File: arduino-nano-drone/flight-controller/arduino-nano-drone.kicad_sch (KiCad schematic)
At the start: 6 parts, among them J1 Conn_01x04_Pin, J2 Conn_01x01_Pin, J3 Conn_01x04_Pin, U1 MPU-6050

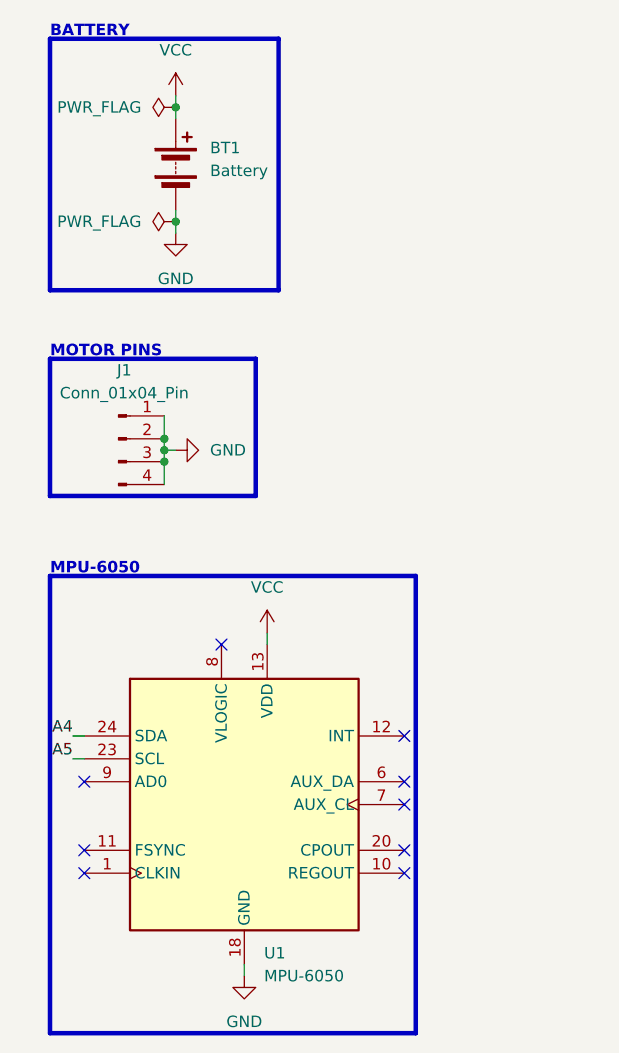
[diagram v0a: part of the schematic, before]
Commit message: project 8 / arduino nano drone / added rt, rr, fl pcb, improved layout
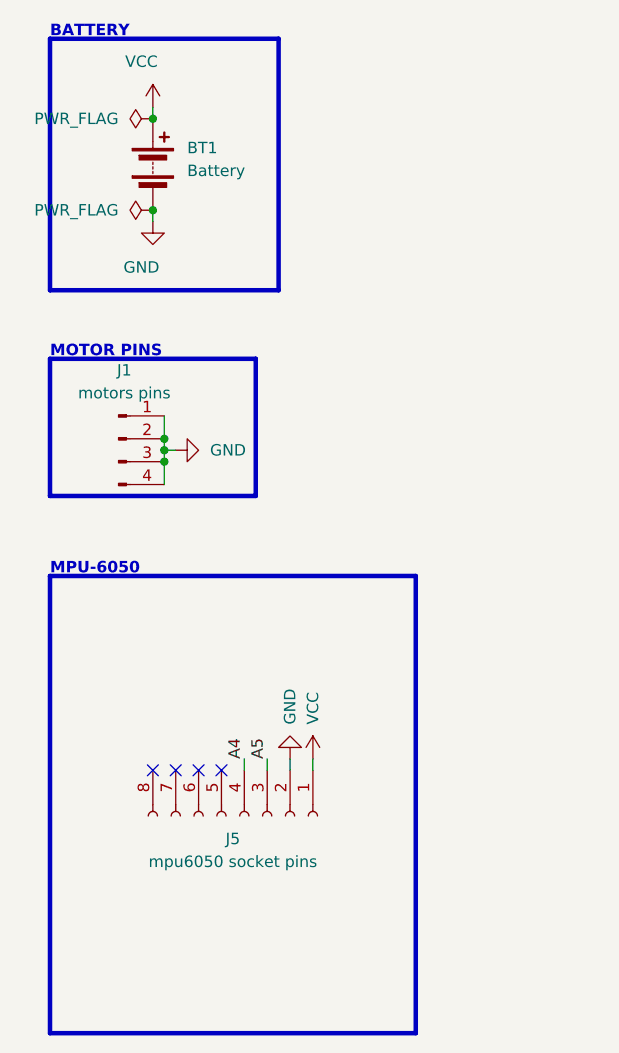
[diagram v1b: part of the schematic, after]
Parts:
- removed U1: MPU-6050, Sensor_Motion:InvenSense_QFN-24_4x4mm_P0.5mm, symbol Sensor_Motion:MPU-6050
- added J5: mpu6050 socket pins, Connector_PinSocket_2.54mm:PinSocket_1x08_P2.54mm_Vertical, symbol Connector:Conn_01x08_Socket
- BT1: footprint (none) -> Connector_PinHeader_2.54mm:PinHeader_1x02_P2.54mm_Vertical
- J1: value Conn_01x04_Pin -> motors pins; footprint (none) -> Connector_PinHeader_2.54mm:PinHeader_1x04_P2.54mm_Vertical
- J2: footprint (none) -> Connector_PinHeader_2.54mm:PinHeader_1x01_P2.54mm_Vertical
- J3: footprint (none) -> Connector_PinHeader_2.54mm:PinHeader_1x04_P2.54mm_Vertical
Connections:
- net A4: now also J5.4 (Pin_4)
- net A5: now also J5.3 (Pin_3)
- net GND: now also J5.2 (Pin_2)
- net VCC: now also J5.1 (Pin_1)
- no-connect marks 29 -> 24

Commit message: Reviewed schematics and boards
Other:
- note added: "Jeśli to I2C, to najprawdopodobniej brakuje Ci pull-upów. Chyba, że moduł je ma."
- note added: "Masa patrzy w dół ;)"
- note added: "Sugeruję nie używać nazw (labelek) typu A4/A5, tylko co to za linia. Strzelam, że I2C, więc np. MPU_SDA/MPU_SCL"
- note added: "Z resztą nawet jak ma, to bezpieczniej dodać i najwyżej nie wlutować :)"
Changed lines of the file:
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@@
     (fill (type none))
+  )
+  (text "Masa patrzy w dół ;)" (at 30.48 59.69 0)
+    (effects (font (size 1.27 1.27) (color 255 32 34 1)) (justify left bottom))
+  )
+  (text "Z resztą nawet jak ma, to bezpieczniej dodać i najwyżej nie wlutować :)"
+    (at 134.62 73.66 0)
+    (effects (font (size 1.27 1.27) (color 255 32 34 1)) (justify left bottom))
   )
   (text "MPU-6050" (at 15.24 76.2 0)
     (effects (font (size 1.27 1.27) (thickness 0.254) bold (color 0 0 0 1)) (justify left bottom))
   )
+  (text "Masa patrzy w dół ;)" (at 41.91 87.63 0)
+    (effects (font (size 1.27 1.27) (color 255 32 34 1)) (justify left bottom))
+  )
   (text "BATTERY" (at 15.24 16.51 0)
     (effects (font (size 1.27 1.27) (thickness 0.254) bold (color 0 0 0 1)) (justify left bottom))
   )
+  (text "Jeśli to I2C, to najprawdopodobniej brakuje Ci pull-upów. Chyba, że moduł je ma."
+    (at 134.62 71.12 0)
+    (effects (font (size 1.27 1.27) (color 255 32 34 1)) (justify left bottom))
+  )
+  (text "Sugeruję nie używać nazw (labelek) typu A4/A5, tylko co to za linia. Strzelam, że I2C, więc np. MPU_SDA/MPU_SCL"
+    (at 35.56 93.98 0)
+    (effects (font (size 1.27 1.27) (color 255 32 34 1)) (justify left bottom))
+  )
   (text "MOTOR PINS" (at 15.24 52.07 0)

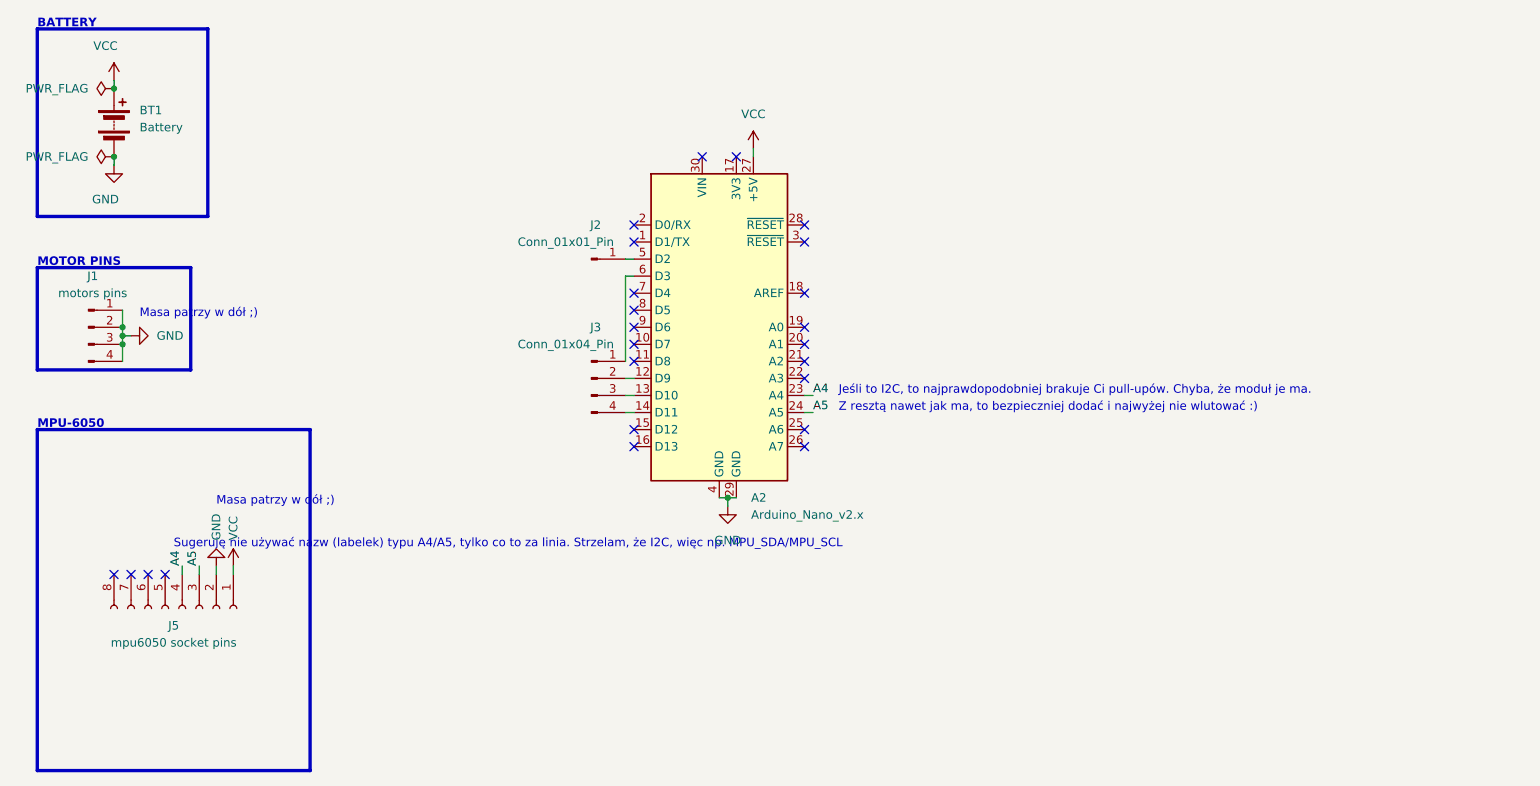
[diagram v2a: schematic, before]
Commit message: project 8 / arduino nano drone / improved schematics and pcb layout
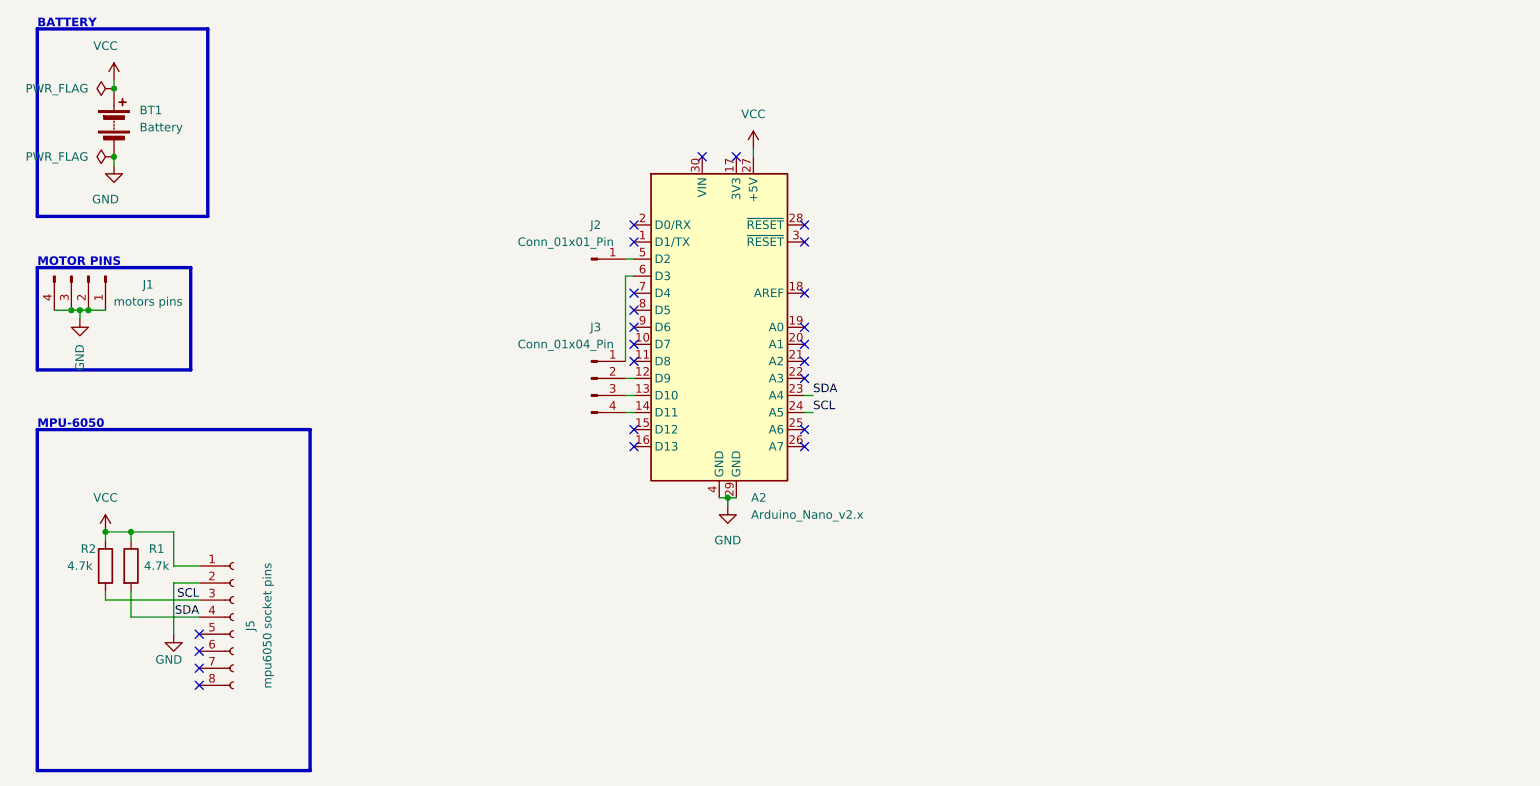
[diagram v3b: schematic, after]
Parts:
- added R1, R2: 4.7k, Resistor_THT:R_Axial_DIN0204_L3.6mm_D1.6mm_P7.62mm_Horizontal, symbol Device:R
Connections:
- net VCC: now also R1.1, R2.1
- net A4 renamed SDA
- net SDA: now also R1.2
- net A5 renamed SCL
- net SCL: now also R2.2
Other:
- note removed: "Jeśli to I2C, to najprawdopodobniej brakuje Ci pull-upów. Chyba, że moduł je ma."
- note removed: "Masa patrzy w dół ;)"
- note removed: "Sugeruję nie używać nazw (labelek) typu A4/A5, tylko co to za linia. Strzelam, że I2C, więc np. MPU_SDA/MPU_SCL"
- note removed: "Z resztą nawet jak ma, to bezpieczniej dodać i najwyżej nie wlutować :)"
- moved on the sheet: J1, J5
